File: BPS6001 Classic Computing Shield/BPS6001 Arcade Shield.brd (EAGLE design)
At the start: 95.2 x 53.3 mm, 46 parts, among them J1 CON_PS/2, J2 CON_PS/2, J3 AUDIO-CONNECTOR-6P-SMD-344003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, U1 AMEGA_SHIELD_NOANALOGNO_ANALOG

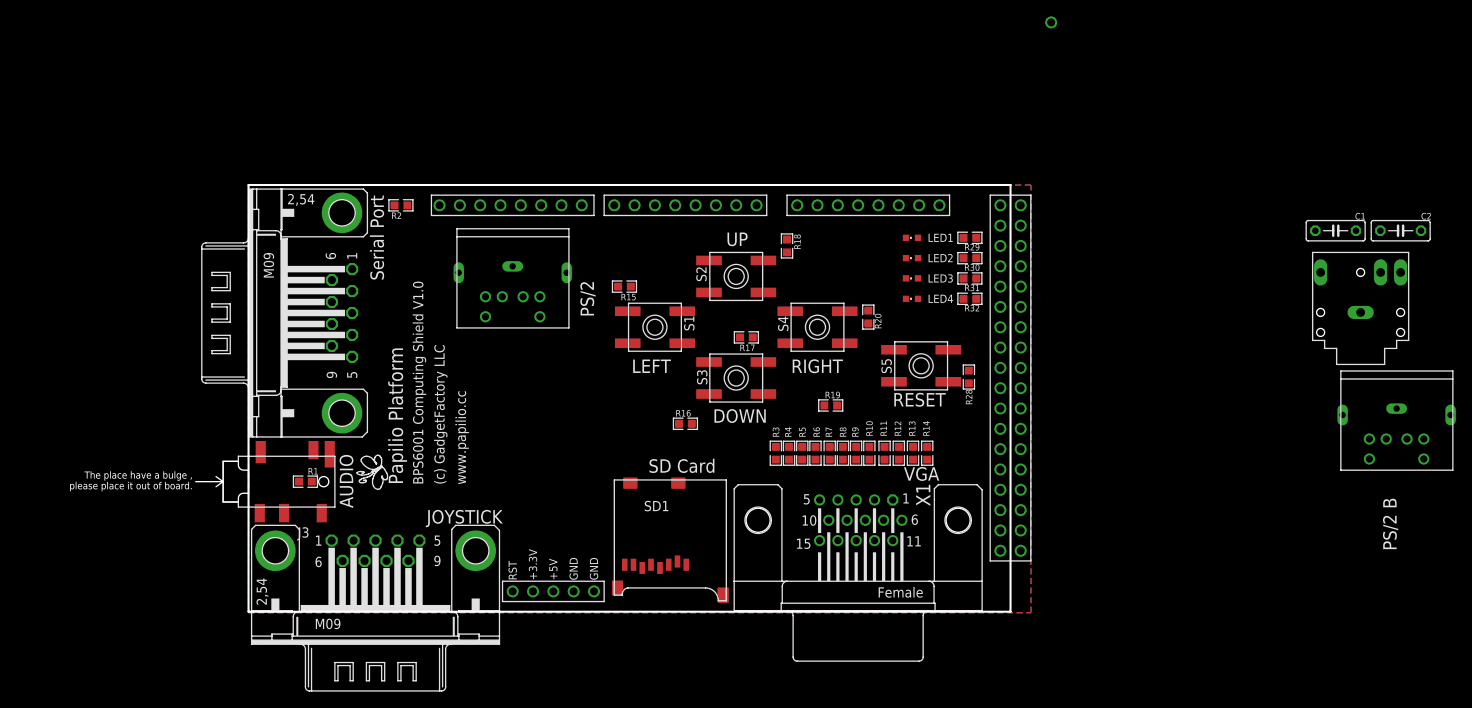
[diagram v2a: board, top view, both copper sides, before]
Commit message: Major rework with all sections separated out.
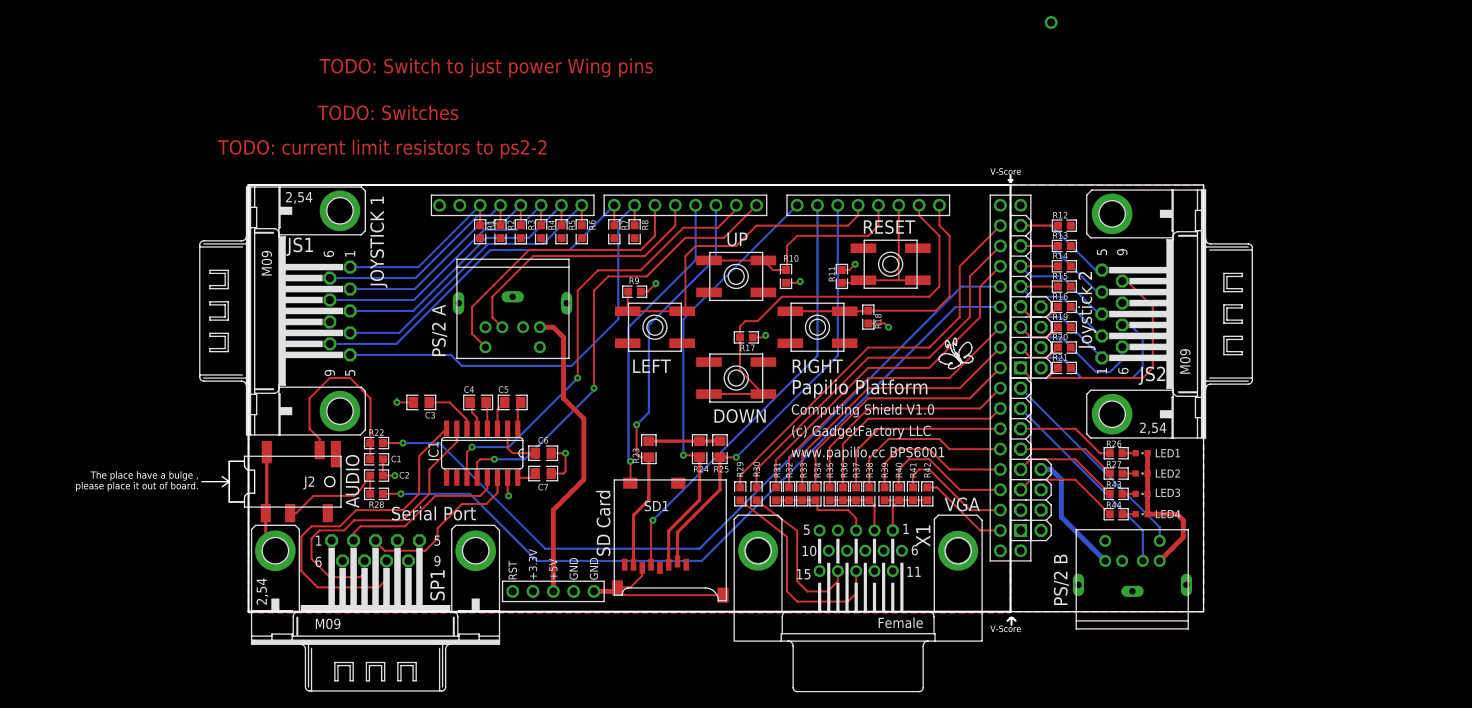
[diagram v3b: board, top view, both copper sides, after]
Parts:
- removed AUDIO: AUDIOJACK, GadgetFactory:AUDJCK
- added AH1, AL: WING8WING8_NOHOLES, Papilio:WINGSIDE_8BIT_NOHOLES
- added C3, C4, C5, C6, C7: .1uF, GadgetFactory_6.0:0805
- added IC1: MAX3232CSE, maxim:SO16
- added R21: 47K, GadgetFactory:0603
- added R22: 3.3K, GadgetFactory:0603
- added R23, R24, R25: 50K, GadgetFactory_6.0:0805
- added R26, R27, R43, R44: 390, GadgetFactory:0603
- added R33, R37, R40: 1K, GadgetFactory:0603
- added R34, R38, R39: 510, GadgetFactory:0603
- added R35, R42: 3.9K, GadgetFactory:0603
- added R36, R41: 2K, GadgetFactory:0603
- added SP1: (no value), con-subd:M09HP
- C1, C2: device resistor:C050-025X075 -> GadgetFactory:0603
- J2: value CON_PS/2 -> AUDIO-CONNECTOR-6P-SMD-3440030P1; device usb1:PS/2 -> OPL Eagle Library:6P-SMD-3.5
- J3: value AUDIO-CONNECTOR-6P-SMD-3440030P1 -> CON_PS/2; device OPL Eagle Library:6P-SMD-3.5 -> usb1:PS/2
- R1, R2: value 82.5 -> 47K
- R10, R11, R6: value 510 -> 47K
- R12, R5, R9: value 1K -> 47K
- R13, R4, R8: value 2K -> 47K
- R14, R3, R7: value 3.9K -> 47K
- R16, R19: value 3.3K -> 47K
- R28: value 47K -> 3.3K
- R29, R30: value 390 -> 82.5
- R31: value 390 -> 3.9K
- R32: value 390 -> 2K
- X1: device con-subd:HDF15H -> GadgetFactory_6.0:HDF15H
- moved J2 139.0 mm to (4.57, 16.3), turned to 180 degrees
- moved C2 131.6 mm to (16.0, 17.0), turned to 0 degrees
- moved C1 123.2 mm to (16.0, 19.1)
- moved J3 107.1 mm to (110.5, 6.35)
- moved JS2 96.3 mm to (108.0, 37.2), turned to 90 degrees
- moved R28 75.5 mm to (16.0, 14.7), turned to 0 degrees
- moved LOGO1 73.9 mm to (88.5, 31.8), turned to 0 degrees
- moved R15 55.0 mm to (102.0, 40.6), turned to 0 degrees
- moved R16 49.6 mm to (102.0, 38.1)
- moved R29 43.0 mm to (61.5, 14.7), turned to 270 degrees
- moved R3 42.2 mm to (34.0, 47.5)
- moved R4 41.6 mm to (36.6, 47.5)
- moved R5 40.9 mm to (39.1, 47.5)
- moved R6 40.2 mm to (41.7, 47.5)
- moved R30 39.7 mm to (63.5, 14.7), turned to 270 degrees
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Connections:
- removed net AUDIO+: C2.1, R19.2, U1.D20
- removed net AUDIO-: C1.1, R16.2, U1.D19
- removed net N$1: J3.L, R16.1
- removed net N$16: JS2.1
- removed net N$17: JS2.2
- removed net N$18: JS2.3
- removed net N$21: JS2.9
- removed net NC1: U1.D4
- removed net NC2: U1.D3
- removed net SD_DI: SD1.3
- removed net SD_DO: SD1.7
- removed net SW1: R15.2, S1.A, S1.A', U1.D2
- removed net SW2: R18.2, S2.A, S2.A', U1.D15
- removed net SW3: R17.2, S3.A, S3.A', U1.D16
- removed net SW4: R20.2, S4.A, S4.A', U1.D17
- new net 5V0_PS2: AH1.5V@2, J3.4
- new net AUDIO-LEFT: R22.2, U1.D28
- new net AUDIO-RIGHT: R28.2, U1.D30
- new net CTS: IC1.9
- new net DTE_CTS: IC1.8, SP1.8
- new net DTE_RTS: IC1.7, SP1.7
- new net DTE_RX: IC1.13, SP1.2
- new net DTE_TX: IC1.14, SP1.3
- new net JOY_3V3: AH1.3V3@2, AL.3V3@2, R12.2, R13.2, R14.2, R15.2, R16.2, R19.2, R20.2, R21.2
- new net JOY_GND: AH1.GND@2, AL.GND@2, J3.3, JS2.8, LED1.C, LED2.C, LED3.C, LED4.C, U1.GND@4
- new net JS1_1: JS1.1, R1.1, U1.D13
- new net JS1_2: JS1.2, R3.1, U1.D11
- new net JS1_3: JS1.3, R5.1, U1.D9
- new net JS1_4: JS1.4, R6.1, U1.D8
- new net JS1_5: JS1.5, R8.1, U1.D6
- new net JS1_6: JS1.6, R2.1, U1.D12
- new net JS1_7: JS1.7, R4.1, U1.D10
- new net JS1_9: JS1.9, R7.1, U1.D7
- new net JS2_7: AL.1, JS2.7, R20.1, U1.D35
- new net LED5: AH1.1, U1.D51
- new net LED6: AH1.0, U1.D53
- new net N$12: C4.2, IC1.4
- new net N$13: C5.1, IC1.3
- new net N$14: C4.1, IC1.5
- new net N$34: C2.1, J2.R, R28.1
- new net N$6: C6.1, IC1.2
- new net N$7: C3.1, IC1.6
- new net N$8: C5.2, IC1.1
- new net RTS: IC1.10
- new net SD_CD: SD1.CD1, U1.D3
- new net SD_MISO: R23.1, SD1.7, U1.D2
- new net SD_MOSI: R24.1, SD1.3, U1.D14
- new net SW_DOWN: R17.2, S4.A, S4.A', U1.D20
- new net SW_LEFT: R9.2, S3.A, S3.A', U1.D17
- new net SW_RIGHT: R18.2, S5.A, S5.A', U1.D21
- new net SW_UP: R10.2, S1.A, S1.A', U1.D18
- net 3V3: now also C7.1, IC1.16, R1.2, R2.2, R23.2, R24.2, R25.2, R3.2, R4.2, R5.2, R6.2, R7.2, R8.2
- net 5V0: no longer J2.4, JS1.7, U1.5V@1
- net BLUE: now also R31.2, R32.2, R33.2, R34.2; no longer R3.2, R4.2, R5.2, R6.2
- net BLUE1: now also R31.1, U1.D26; no longer R3.1, U1.D30
- net BLUE2: now also R32.1; no longer R4.1
- net BLUE3: now also R33.1; no longer R5.1
- net BLUE4: now also R34.1; no longer R6.1
- net GND: now also C3.2, C6.2, C7.2, IC1.15, J2.COM1, J2.COM2, R10.1, R11.1, R9.1, SP1.5, SP1.G1, SP1.G2; no longer AUDIO.1, J2.3, LED1.C, LED2.C, LED3.C, LED4.C, R15.1, R20.1, R28.1, U1.GND@4
- net GREEN: now also R35.2, R36.2, R37.2, R38.2; no longer R10.2, R7.2, R8.2, R9.2
- net GREEN1: now also R35.1; no longer R7.1
- net GREEN2: now also R36.1; no longer R8.1
- net GREEN3: now also R37.1; no longer R9.1
- net GREEN4: now also R38.1; no longer R10.1
- net HORIZONTAL_SYNC: now also R29.1, U1.D22; no longer R1.1, U1.D21
- net JS2_1: now also AL.3, JS2.1, R16.1, U1.D31; no longer JS1.1, U1.D13
- net JS2_2: now also AL.4, JS2.2, R15.1, U1.D29; no longer JS1.2, U1.D11
- net JS2_3: now also AL.5, JS2.3, R14.1, U1.D27; no longer JS1.3, U1.D10
- net JS2_4: now also AL.6, JS2.4, R13.1, U1.D25; no longer JS1.4, U1.D9
- net JS2_5: now also AL.7, JS2.5, R12.1, U1.D23; no longer JS1.5, U1.D7
- net JS2_6: now also AL.2, JS2.6, R19.1, U1.D33; no longer JS1.6, U1.D12
- net JS2_9: now also AL.0, JS2.9, R21.1, U1.D37; no longer JS1.9, U1.D8
- net LED1: now also AH1.5, R26.2, U1.D43; no longer R29.2, U1.D22
- net LED2: now also AH1.4, R27.2, U1.D45; no longer R30.2, U1.D24
- net LED3: now also AH1.3, R43.2, U1.D47; no longer R31.2, U1.D26
- net LED4: now also AH1.2, R44.2, U1.D49; no longer R32.2, U1.D28
- net N$10: now also R27.1; no longer R30.1
- net N$11: now also R26.1; no longer R29.1
- net N$2: now also C1.1, J2.L, R22.1; no longer J3.R, R19.1
- net N$3: now also R44.1; no longer R32.1
- net N$4: now also R29.2; no longer R1.2
- net N$5: now also R30.2; no longer R2.2
- net N$9: now also R43.1; no longer R31.1
- net PS2CLK1: now also U1.D5; no longer U1.D6
- net PS2CLK2: now also AH1.7, J3.5, U1.D39; no longer J2.5
- net PS2DAT1: now also U1.D4; no longer U1.D5
- net PS2DAT2: now also AH1.6, J3.1, U1.D41; no longer J2.1
- net RED: now also R39.2, R40.2, R41.2, R42.2; no longer R11.2, R12.2, R13.2, R14.2
- net RED1: now also R42.1; no longer R14.1
- net RED2: now also R41.1; no longer R13.1
- net RED3: now also R40.1; no longer R12.1
- net RED4: now also R39.1; no longer R11.1
- net RESET: now also R11.2, S2.A, S2.A', U1.D19; no longer R28.2, S5.A, S5.A', U1.D18
- net RX: now also IC1.12; no longer JS2.5
- net SD_!CS: now also R25.1, U1.D16
- net SD_SCK: now also U1.D15
- net TX: now also IC1.11; no longer JS2.4
- net VERTICAL_SYNC: now also R30.1, U1.D24; no longer R2.1, U1.D14
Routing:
- net AUDIO-LEFT: track 0.00 -> 96.2 mm, vias 0 -> 1
- net AUDIO-RIGHT: track 0.00 -> 93.8 mm, vias 0 -> 1
- net GND: track 0.00 -> 61.0 mm, vias 0 -> 9
- net RX: track 0.00 -> 57.5 mm, vias 0 -> 2
- net TX: track 0.00 -> 56.3 mm, vias 0 -> 2
- net SW_DOWN: track 0.00 -> 54.8 mm
- net SD_MOSI: track 0.00 -> 54.3 mm, vias 0 -> 1
- net JS1_5: track 0.00 -> 54.1 mm
- net SD_!CS: track 0.00 -> 54.0 mm, vias 0 -> 1
- net SD_SCK: track 0.00 -> 53.5 mm, vias 0 -> 1
- net SD_MISO: track 0.00 -> 51.1 mm, vias 0 -> 1
- net HORIZONTAL_SYNC: track 0.00 -> 50.7 mm
- net VERTICAL_SYNC: track 0.00 -> 47.3 mm
- net JS1_9: track 0.00 -> 45.2 mm
- net DTE_CTS: track 0.00 -> 45.0 mm
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- added copper zone on layer 1, net JOY_3V3
- added copper zone on layer 16, net JOY_GND
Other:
- board size 95.2 x 53.3 mm -> 119.4 x 56.1 mm
- board text added: "Computing Shield V1.0"
- board text added: "JOYSTICK 1"
- board text added: "Joystick 2"
- board text added: "PS/2 A"
- board text added: "TODO: Switch to just power Wing pins"
- board text added: "TODO: Switches"
- board text added: "TODO: current limit resistors to ps2-2"
- board text added: "V-Score"
- board text added: "www.papilio.cc BPS6001"
- board text removed: "BPS6001 Computing Shield V1.0"
- board text removed: "JOYSTICK"
- board text removed: "PS/2"
- board text removed: "www.papilio.cc"

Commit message: 2nd Audio Jack, Mounting Holes
Moved the Joystick ports to the same side, I'm considering rotating the
whole thing 180 degrees so the joysticks are on the bottom...
Added a second audio jack to the 16 bit Wing.
The first audio jack is now connected to the Analog input pins of the
atmel chip and also to FPGA pins. This is for reading data off tape
drives or recording audio.
Added mounting holes.
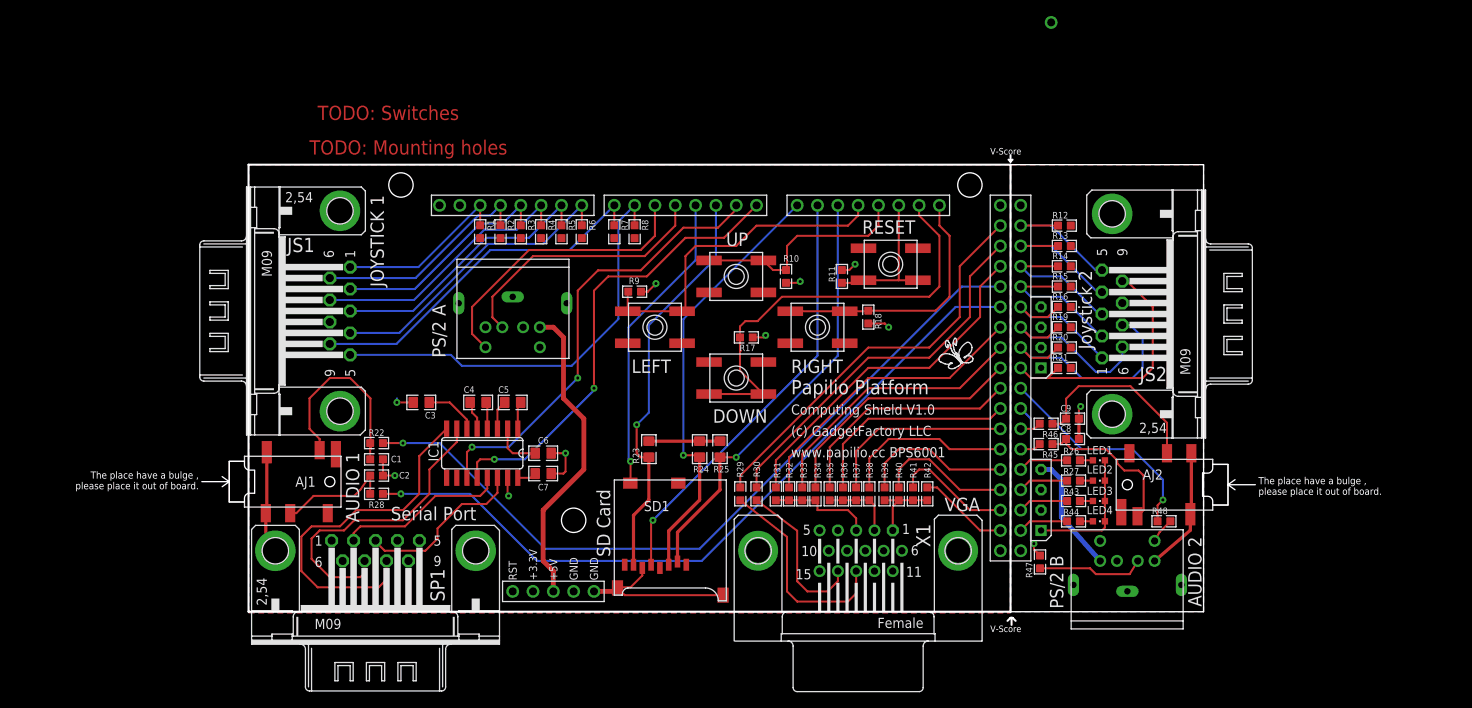
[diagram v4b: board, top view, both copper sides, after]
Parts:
- removed AH1, AL: WING8WING8_NOHOLES, Papilio:WINGSIDE_8BIT_NOHOLES
- removed J3: CON_PS/2, usb1:PS/2
- added AJ2: AUDIO-CONNECTOR-6P-SMD-3440030P1, OPL Eagle Library:6P-SMD-3.5
- added C8, C9: 4.7nF, GadgetFactory:0603
- added PS2_B: CON_PS/2, usb1:PS/2
- added PWR_1, PWR_2: POWER_ONLYNOTEXT, Papilio:POWER_NO_TEXT
- added R45, R46: 3.3K, GadgetFactory:0603
- added R47, R48: 390, GadgetFactory_6.0:0603
- added U$1, U$2, U$3: (no value), GadgetFactory_Pub:STAND-OFF-TIGHT
- moved R26 5.41 mm to (103.1, 18.9)
- moved R27 5.41 mm to (103.1, 16.4)
- moved R43 5.41 mm to (103.1, 13.8)
- moved R44 5.41 mm to (103.1, 11.3)
- moved LED1 5.41 mm to (106.3, 18.9)
- moved LED2 5.41 mm to (106.3, 16.4)
- moved LED3 5.41 mm to (106.3, 13.8)
- moved LED4 5.41 mm to (106.3, 11.3)
- renumbered J1 to PS2_A, J2 to AJ1
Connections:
- net AUDIO-LEFT renamed AUDIO1-LEFT
- net AUDIO-RIGHT renamed AUDIO1-RIGHT
- removed net LED5: AH1.1, U1.D51
- removed net LED6: AH1.0, U1.D53
- new net AUDIO2-LEFT: R45.2, U1.D45
- new net AUDIO2-RIGHT: R46.2, U1.D43
- new net N$1: AJ2.L, C8.1, R45.1
- new net N$15: AJ2.R, C9.1, R46.1
- new net N$16: PS2_B.1, R47.2
- new net N$17: PS2_B.5, R48.2
- net 5V0_PS2: now also PS2_B.4, PWR_2.P4; no longer AH1.5V@2, J3.4
- net JOY_3V3: now also PWR_1.P3; no longer AH1.3V3@2, AL.3V3@2
- net JOY_GND: now also AJ2.COM1, AJ2.COM2, C8.2, C9.2, PS2_B.3, PWR_1.P1, PWR_2.P1; no longer AH1.GND@2, AL.GND@2, J3.3
- net JS2_1: no longer AL.3
- net JS2_2: no longer AL.4
- net JS2_3: no longer AL.5
- net JS2_4: no longer AL.6
- net JS2_5: no longer AL.7
- net JS2_6: no longer AL.2
- net JS2_7: no longer AL.1
- net JS2_9: no longer AL.0
- net LED1: now also U1.D47; no longer AH1.5, U1.D43
- net LED2: now also U1.D49; no longer AH1.4, U1.D45
- net LED3: now also U1.D51; no longer AH1.3, U1.D47
- net LED4: now also U1.D53; no longer AH1.2, U1.D49
- net PS2CLK2: now also R48.1; no longer AH1.7, J3.5
- net PS2DAT2: now also R47.1; no longer AH1.6, J3.1
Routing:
- net N$15: track 0.00 -> 23.4 mm
- net N$1: track 0.00 -> 19.5 mm
- net JOY_GND: track 18.7 -> 36.6 mm, vias 0 -> 1
- net N$16: track 0.00 -> 13.4 mm
- net LED4: track 13.5 -> 6.28 mm
- net LED3: track 13.5 -> 6.28 mm
- net LED2: track 12.4 -> 6.28 mm
- net LED1: track 12.4 -> 6.28 mm
- net PS2DAT2: track 25.4 -> 19.4 mm, vias 0 -> 1
- net N$17: track 0.00 -> 3.17 mm
- net AUDIO2-RIGHT: track 0.00 -> 2.64 mm
- net AUDIO2-LEFT: track 0.00 -> 2.64 mm
- net PS2CLK2: track 26.3 -> 28.0 mm, vias 0 -> 1
- net 5V0: track 37.9 -> 38.9 mm
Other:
- board size 119.4 x 56.1 mm -> 119.4 x 58.7 mm
- board text added: "AUDIO 1"
- board text added: "AUDIO 2"
- board text added: "TODO: Mounting holes"
- board text removed: "AUDIO"
- board text removed: "TODO: Switch to just power Wing pins"
- board text removed: "TODO: current limit resistors to ps2-2"
